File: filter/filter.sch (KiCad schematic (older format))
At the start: 10 parts, among them J101 TRX, J102 TRX

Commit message: filter backup
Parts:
- C101: value C -> 1p
- C102: value C -> 330p
- C103: value C -> 1000p
- C104: value C -> 360p
- C105: value C -> 620p
- C106: value C -> 470p
- L101: value T37 -> 675n
- L102: value T37 -> 243n
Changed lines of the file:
@@
 P 5250 3500
 F 0 "L101" V 5440 3500 50  0000 C CNN
-F 1 "T37" V 5349 3500 50  0000 C CNN
+F 1 "675n" V 5349 3500 50  0000 C CNN
 F 2 "Inductor_THT:L_Toroid_Horizontal_D9.5mm_P15.00mm_Diameter10-5mm_Amidon-T37" H 5250 3500 50  0001 C CNN
 F 3 "~" H 5250 3500 50  0001 C CNN
@@
 P 5000 3750
 F 0 "C104" H 5115 3796 50  0000 L CNN
-F 1 "C" H 5115 3705 50  0000 L CNN
+F 1 "360p" H 5115 3705 50  0000 L CNN
 F 2 "Capacitor_SMD:C_0805_2012Metric_Pad1.18x1.45mm_HandSolder" H 5038 3600 50  0001 C CNN
 F 3 "~" H 5000 3750 50  0001 C CNN
@@
 P 5750 3500
 F 0 "C103" V 5498 3500 50  0000 C CNN
-F 1 "C" V 5589 3500 50  0000 C CNN
+F 1 "1000p" V 5589 3500 50  0000 C CNN
 F 2 "Capacitor_SMD:C_0805_2012Metric_Pad1.18x1.45mm_HandSolder" H 5788 3350 50  0001 C CNN
 F 3 "~" H 5750 3500 50  0001 C CNN
@@
 P 5750 3000
 F 0 "C101" V 5498 3000 50  0000 C CNN
-F 1 "C" V 5589 3000 50  0000 C CNN
+F 1 "1p" V 5589 3000 50  0000 C CNN
 F 2 "Capacitor_SMD:C_0805_2012Metric_Pad1.18x1.45mm_HandSolder" H 5788 2850 50  0001 C CNN
 F 3 "~" H 5750 3000 50  0001 C CNN
@@
 P 6000 3750
 F 0 "C105" H 5885 3704 50  0000 R CNN
-F 1 "C" H 5885 3795 50  0000 R CNN
+F 1 "620p" H 5885 3795 50  0000 R CNN
 F 2 "Capacitor_SMD:C_0805_2012Metric_Pad1.18x1.45mm_HandSolder" H 6038 3600 50  0001 C CNN
 F 3 "~" H 6000 3750 50  0001 C CNN
@@
 P 6250 3500
 F 0 "L102" V 6440 3500 50  0000 C CNN
-F 1 "T37" V 6349 3500 50  0000 C CNN
+F 1 "243n" V 6349 3500 50  0000 C CNN
 F 2 "Inductor_THT:L_Toroid_Horizontal_D9.5mm_P15.00mm_Diameter10-5mm_Amidon-T37" H 6250 3500 50  0001 C CNN
 F 3 "~" H 6250 3500 50  0001 C CNN
@@
 P 6250 3000
 F 0 "C102" V 6502 3000 50  0000 C CNN
-F 1 "C" V 6411 3000 50  0000 C CNN
+F 1 "330p" V 6411 3000 50  0000 C CNN
 F 2 "Capacitor_SMD:C_0805_2012Metric_Pad1.18x1.45mm_HandSolder" H 6288 2850 50  0001 C CNN
 F 3 "~" H 6250 3000 50  0001 C CNN
@@
 P 6500 3750
 F 0 "C106" H 6385 3704 50  0000 R CNN
-F 1 "C" H 6385 3795 50  0000 R CNN
+F 1 "470p" H 6385 3795 50  0000 R CNN
 F 2 "Capacitor_SMD:C_0805_2012Metric_Pad1.18x1.45mm_HandSolder" H 6538 3600 50  0001 C CNN
 F 3 "~" H 6500 3750 50  0001 C CNN

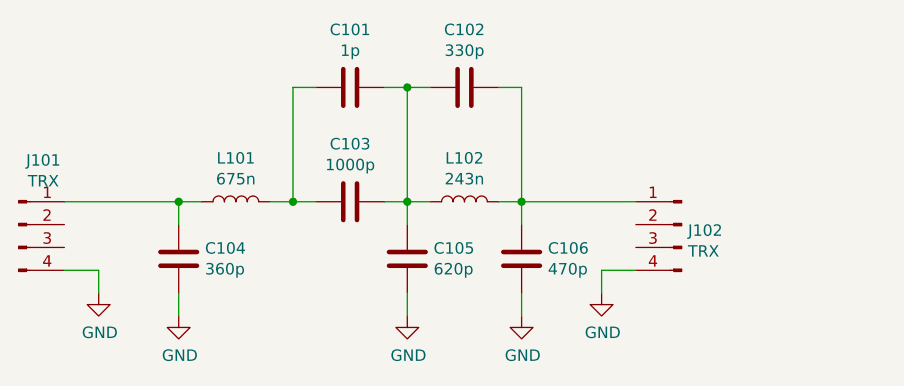
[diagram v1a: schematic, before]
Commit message: Filter updated
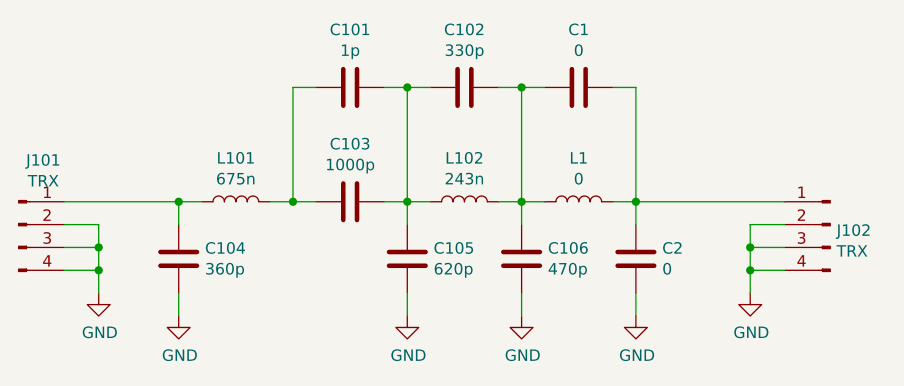
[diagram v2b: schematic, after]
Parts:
- added C1, C2: 0, Capacitor_SMD:C_0805_2012Metric_Pad1.18x1.45mm_HandSolder, symbol Device:C
- added L1: 0, Inductor_THT:L_Toroid_Horizontal_D9.5mm_P15.00mm_Diameter10-5mm_Amidon-T37, symbol Device:L
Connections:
- net GND: now also J101.2 (Pin_2), J101.3 (Pin_3), J102.2 (Pin_2), J102.3 (Pin_3), C2.1
- net at C102.2, C106.2, L102.2: now also C1.1, L1.1; no longer J102.1 (Pin_1)
- new net: C1.2, C2.2, J102.1 (Pin_1), L1.2
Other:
- moved on the sheet: J102
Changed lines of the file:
@@
 	6500 4000 6500 3900
-Wire Wire Line
-	7000 3500 6500 3500
 Wire Wire Line
 	5000 3500 4500 3500
@@
 L power:GND #PWR0102
 U 1 1 61019A2B
-P 6850 3900
-F 0 "#PWR0102" H 6850 3650 50  0001 C CNN
-F 1 "GND" H 6855 3727 50  0000 C CNN
-F 2 "" H 6850 3900 50  0001 C CNN
-F 3 "" H 6850 3900 50  0001 C CNN
-	1    6850 3900
+P 7500 3900
+F 0 "#PWR0102" H 7500 3650 50  0001 C CNN
+F 1 "GND" H 7505 3727 50  0000 C CNN
+F 2 "" H 7500 3900 50  0001 C CNN
+F 3 "" H 7500 3900 50  0001 C CNN
+	1    7500 3900
 	1    0    0    -1
 $EndComp
 Wire Wire Line
-	6850 3900 6850 3800
+	7500 3900 7500 3800
 Wire Wire Line
-	6850 3800 7000 3800
+	7500 3800 7650 3800
 $Comp
 L Connector:Conn_01x04_Male J101
@@
 L Connector:Conn_01x04_Male J102
 U 1 1 61024C76
-P 7200 3600
-F 0 "J102" H 7172 3574 50  0000 R CNN
-F 1 "TRX" H 7172 3483 50  0000 R CNN
-F 2 "Connector_PinHeader_2.54mm:PinHeader_1x04_P2.54mm_Vertical" H 7200 3600 50  0001 C CNN
-F 3 "~" H 7200 3600 50  0001 C CNN
-	1    7200 3600
+P 7850 3600
+F 0 "J102" H 7822 3574 50  0000 R CNN
+F 1 "TRX" H 7822 3483 50  0000 R CNN
+F 2 "Connector_PinHeader_2.54mm:PinHeader_1x04_P2.54mm_Vertical" H 7850 3600 50  0001 C CNN
+F 3 "~" H 7850 3600 50  0001 C CNN
+	1    7850 3600
 	-1   0    0    -1
 $EndComp
+$Comp
+L Device:L L1
+U 1 1 60DD4EB1
+P 6750 3500
+F 0 "L1" V 6940 3500 50  0000 C CNN
+F 1 "0" V 6849 3500 50  0000 C CNN
+F 2 "Inductor_THT:L_Toroid_Horizontal_D9.5mm_P15.00mm_Diameter10-5mm_Amidon-T37" H 6750 3500 50  0001 C CNN
+F 3 "~" H 6750 3500 50  0001 C CNN
+	1    6750 3500
+	0    -1   -1   0
+$EndComp
+$Comp
+L Device:C C1
+U 1 1 60DD4EB7
+P 6750 3000
+F 0 "C1" V 7002 3000 50  0000 C CNN
+F 1 "0" V 6911 3000 50  0000 C CNN
+F 2 "Capacitor_SMD:C_0805_2012Metric_Pad1.18x1.45mm_HandSolder" H 6788 2850 50  0001 C CNN
+F 3 "~" H 6750 3000 50  0001 C CNN
+	1    6750 3000
+	0    -1   -1   0
+$EndComp
+$Comp
+L Device:C C2
+U 1 1 60DD4EBD
+P 7000 3750
+F 0 "C2" H 6885 3704 50  0000 R CNN
+F 1 "0" H 6885 3795 50  0000 R CNN
+F 2 "Capacitor_SMD:C_0805_2012Metric_Pad1.18x1.45mm_HandSolder" H 7038 3600 50  0001 C CNN
+F 3 "~" H 7000 3750 50  0001 C CNN
+	1    7000 3750
+	-1   0    0    1
+$EndComp
+Wire Wire Line
+	6900 3500 7000 3500
+Wire Wire Line
+	7000 3500 7000 3600
+Wire Wire Line
+	6900 3000 7000 3000
+Wire Wire Line
+	7000 3000 7000 3500
+Connection ~ 7000 3500
+$Comp
+L power:GND #PWR01
+U 1 1 60DD4EC8
+P 7000 4000
+F 0 "#PWR01" H 7000 3750 50  0001 C CNN
+F 1 "GND" H 7005 3827 50  0000 C CNN
+F 2 "" H 7000 4000 50  0001 C CNN
+F 3 "" H 7000 4000 50  0001 C CNN
+	1    7000 4000
+	1    0    0    -1
+$EndComp
+Wire Wire Line
+	7000 4000 7000 3900
+Wire Wire Line
+	6600 3500 6500 3500
+Wire Wire Line
+	6600 3000 6500 3000
+Connection ~ 6500 3000
+Wire Wire Line
+	7000 3500 7650 3500
+Wire Wire Line
+	4500 3600 4650 3600
+Wire Wire Line
+	4650 3600 4650 3700
+Connection ~ 4650 3800
+Wire Wire Line
+	4500 3700 4650 3700
+Connection ~ 4650 3700
+Wire Wire Line
+	4650 3700 4650 3800
+Wire Wire Line
+	7650 3600 7500 3600
+Wire Wire Line
+	7500 3600 7500 3700
+Connection ~ 7500 3800
+Wire Wire Line
+	7650 3700 7500 3700
+Connection ~ 7500 3700
+Wire Wire Line
+	7500 3700 7500 3800
 $EndSCHEMATC
